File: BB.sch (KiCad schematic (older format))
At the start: 0 parts

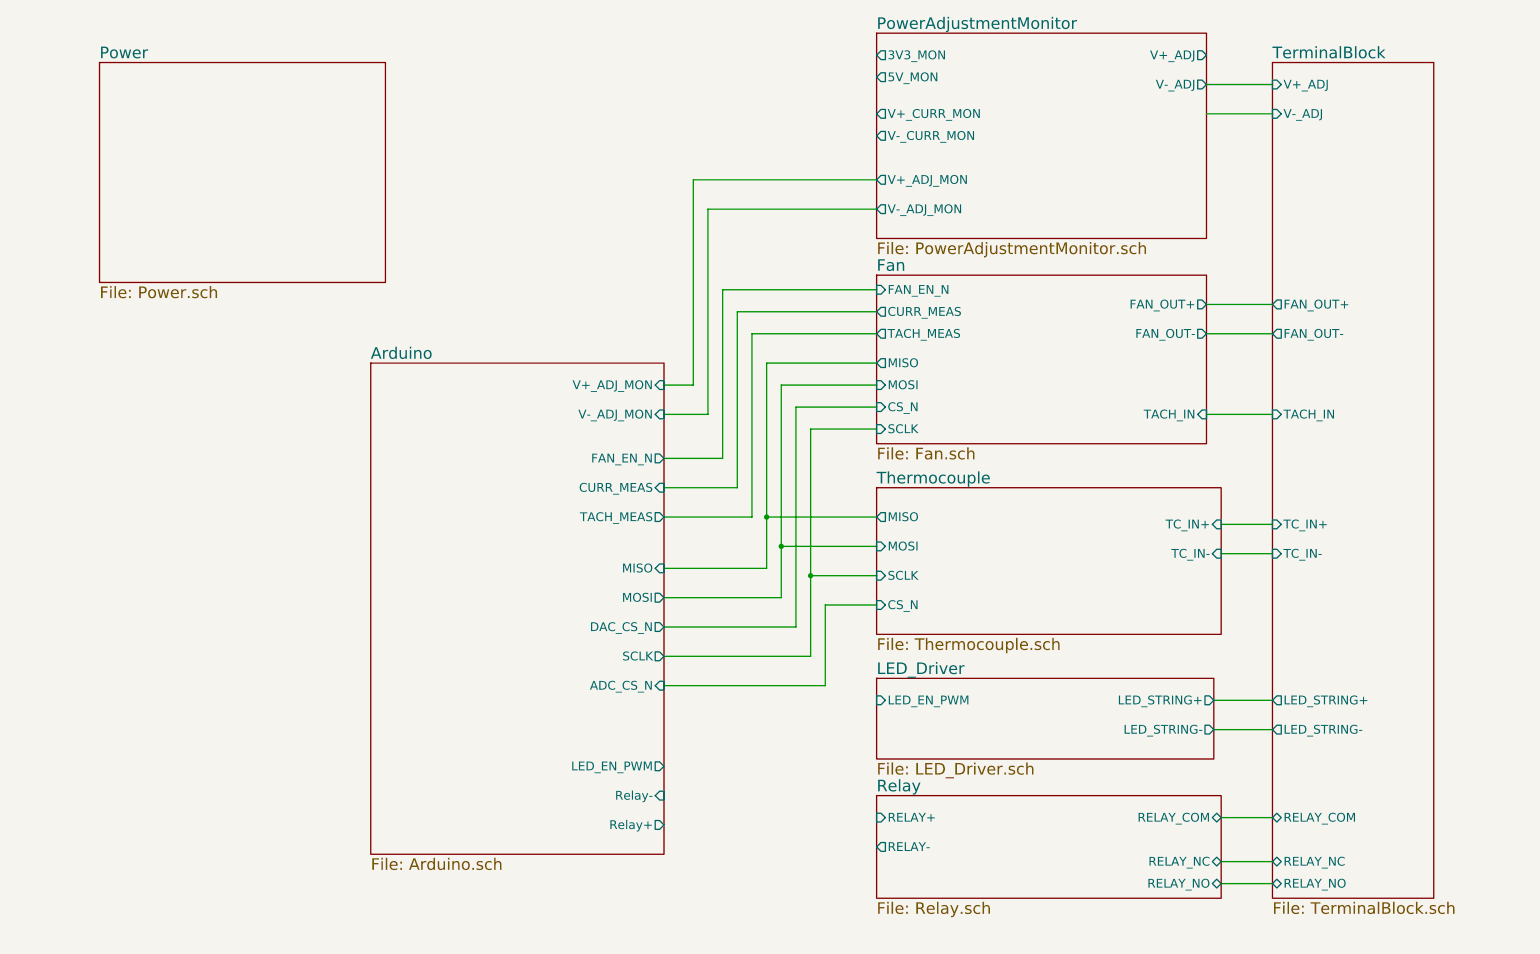
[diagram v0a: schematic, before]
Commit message: Week 3 changes. 	new file:   Arduino.sch 	modified:   BB-cache.lib 	new file:   BB.bck 	new file:   BB.dcm 	new file:   BB.lib 	modified:   BB.sch 	new file:   Fan.sch 	new file:   LED_Driver.sch 	new file:   Power.sch 	new file:   PowerAdjustmentMonitor.sch 	new file:   Relay.sch 	new file:   TerminalBlock.sch 	new file:   Thermocouple.sch
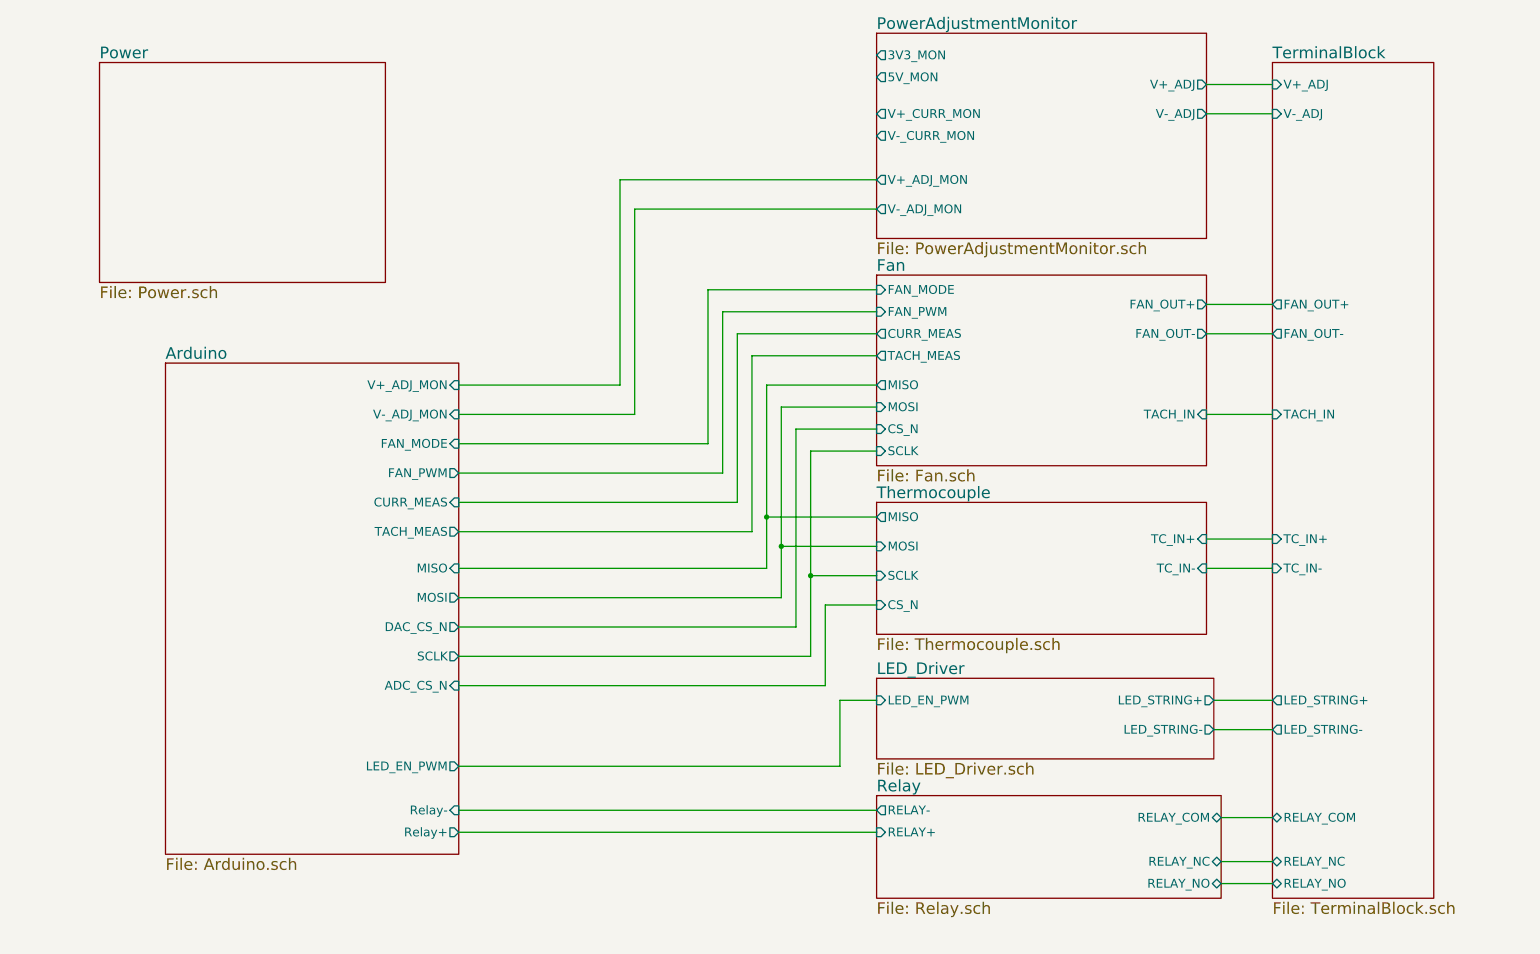
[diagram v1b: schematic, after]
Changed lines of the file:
@@
 F7 "LED_STRING+" O L 9250 5200 60
 F8 "LED_STRING-" O L 9250 5400 60
-F9 "TC_IN+" I L 9250 4000 60
-F10 "TC_IN-" I L 9250 4200 60
+F9 "TC_IN+" I L 9250 4100 60
+F10 "TC_IN-" I L 9250 4300 60
 F11 "RELAY_COM" B L 9250 6000 60
 F12 "RELAY_NC" B L 9250 6300 60
@@
 $EndSheet
 $Sheet
-S 6550 2300 2250 1150
+S 6550 2300 2250 1300
 U 52ED2315
 F0 "Fan" 79
 F1 "Fan.sch" 79
-F2 "SCLK" I L 6550 3350 60
-F3 "CS_N" I L 6550 3200 60
-F4 "MOSI" I L 6550 3050 60
-F5 "MISO" O L 6550 2900 60
+F2 "SCLK" I L 6550 3500 60
+F3 "CS_N" I L 6550 3350 60
+F4 "MOSI" I L 6550 3200 60
+F5 "MISO" O L 6550 3050 60
 F6 "FAN_OUT+" O R 8800 2500 60
 F7 "TACH_IN" I R 8800 3250 60
-F8 "TACH_MEAS" O L 6550 2700 60
-F9 "FAN_EN_N" I L 6550 2400 60
-F10 "CURR_MEAS" O L 6550 2550 60
-F11 "FAN_OUT-" O R 8800 2700 60
+F8 "TACH_MEAS" O L 6550 2850 60
+F9 "CURR_MEAS" O L 6550 2700 60
+F10 "FAN_OUT-" O R 8800 2700 60
+F11 "FAN_PWM" I L 6550 2550 60
+F12 "FAN_MODE" I L 6550 2400 60
 $EndSheet
 $Sheet
@@
 F3 "RELAY_NO" B R 8900 6450 60
 F4 "RELAY_COM" B R 8900 6000 60
-F5 "RELAY+" I L 6550 6000 60
-F6 "RELAY-" O L 6550 6200 60
+F5 "RELAY+" I L 6550 6100 60
+F6 "RELAY-" O L 6550 5950 60
 $EndSheet
 $Sheet
@@
 F0 "PowerAdjustmentMonitor" 79
 F1 "PowerAdjustmentMonitor.sch" 79
-F2 "V+_ADJ" O R 8800 800 60
-F3 "V-_ADJ" O R 8800 1000 60
+F2 "V+_ADJ" O R 8800 1000 60
+F3 "V-_ADJ" O R 8800 1200 60
 F4 "3V3_MON" O L 6550 800 60
 F5 "5V_MON" O L 6550 950 60
@@
 Wire Wire Line
 	8900 6450 9250 6450
-$Sheet
-S 3100 2900 2000 3350
-U 52ED2231
-F0 "Arduino" 79
-F1 "Arduino.sch" 79
-F2 "Relay+" O R 5100 6050 60
-F3 "Relay-" I R 5100 5850 60
-F4 "MOSI" O R 5100 4500 60
-F5 "MISO" I R 5100 4300 60
-F6 "SCLK" O R 5100 4900 60
-F7 "TACH_MEAS" O R 5100 3950 60
-F8 "FAN_EN_N" O R 5100 3550 60
-F9 "CURR_MEAS" I R 5100 3750 60
-F10 "V+_ADJ_MON" I R 5100 3050 60
-F11 "V-_ADJ_MON" I R 5100 3250 60
-F12 "LED_EN_PWM" O R 5100 5650 60
-F13 "DAC_CS_N" O R 5100 4700 60
-F14 "ADC_CS_N" I R 5100 5100 60
-$EndSheet
-Wire Wire Line
-	5100 3050 5300 3050
-Wire Wire Line
-	5100 3250 5400 3250
-Wire Wire Line
-	5300 3050 5300 1650
-Wire Wire Line
-	5300 1650 6550 1650
-Wire Wire Line
-	5400 3250 5400 1850
-Wire Wire Line
-	5400 1850 6550 1850
-Wire Wire Line
-	5100 3550 5500 3550
-Wire Wire Line
-	5500 3550 5500 2400
-Wire Wire Line
-	5500 2400 6550 2400
-Wire Wire Line
-	5100 3750 5600 3750
-Wire Wire Line
-	5600 3750 5600 2550
-Wire Wire Line
-	5600 2550 6550 2550
-Wire Wire Line
-	5100 3950 5700 3950
-Wire Wire Line
-	5700 3950 5700 2700
-Wire Wire Line
-	5700 2700 6550 2700
-Wire Wire Line
-	5100 4300 5800 4300
-Wire Wire Line
-	5800 4300 5800 2900
-Wire Wire Line
-	5800 2900 6550 2900
-Wire Wire Line
-	5100 4500 5900 4500
-Wire Wire Line
-	5900 4500 5900 3050
-Wire Wire Line
-	5900 3050 6550 3050
-Wire Wire Line
-	5100 4700 6000 4700
-Wire Wire Line
-	6000 4700 6000 3200
-Wire Wire Line
-	6000 3200 6550 3200
-Wire Wire Line
-	5100 4900 6100 4900
-Wire Wire Line
-	6100 4900 6100 3350
-Wire Wire Line
-	6100 3350 6550 3350
+Wire Wire Line
+	3700 3050 4800 3050
+Wire Wire Line
+	3700 3250 4900 3250
+Wire Wire Line
+	4800 3050 4800 1650
+Wire Wire Line
+	4800 1650 6550 1650
+Wire Wire Line
+	4900 3250 4900 1850
+Wire Wire Line
+	4900 1850 6550 1850
+Wire Wire Line
+	3700 3650 5500 3650
+Wire Wire Line
+	5500 3650 5500 2550
+Wire Wire Line
+	5500 2550 6550 2550
+Wire Wire Line
+	3700 3850 5600 3850
+Wire Wire Line
+	5600 3850 5600 2700
+Wire Wire Line
+	5600 2700 6550 2700
+Wire Wire Line
+	3700 4050 5700 4050
+Wire Wire Line
+	5700 4050 5700 2850
+Wire Wire Line
+	5700 2850 6550 2850
+Wire Wire Line
+	5800 4300 3700 4300
+Wire Wire Line
+	5800 3050 5800 4300
+Wire Wire Line
+	5800 3050 6550 3050
+Wire Wire Line
+	5900 4500 3700 4500
+Wire Wire Line
+	5900 3200 5900 4500
+Wire Wire Line
+	5900 3200 6550 3200
+Wire Wire Line
+	3700 4700 6000 4700
+Wire Wire Line
+	6000 4700 6000 3350
+Wire Wire Line
+	6000 3350 6550 3350
+Wire Wire Line
+	6100 4900 3700 4900
+Wire Wire Line
+	6100 3500 6100 4900
+Wire Wire Line
+	6100 3500 6550 3500
 Wire Wire Line
 	6550 4550 6200 4550
@@
 	6200 4550 6200 5100
 Wire Wire Line
-	6200 5100 5100 5100
-Wire Wire Line
-	9250 4000 8900 4000
-Wire Wire Line
-	9250 4200 8900 4200
+	6200 5100 3700 5100
 Wire Wire Line
 	9250 5200 8850 5200
@@
 	9250 5400 8850 5400
 $Sheet
-S 6550 3750 2350 1000
+S 6550 3850 2250 900
 U 52ED22BF
 F0 "Thermocouple" 79
@@
 F4 "SCLK" I L 6550 4350 60
 F5 "CS_N" I L 6550 4550 60
-F6 "TC_IN+" I R 8900 4000 60
-F7 "TC_IN-" I R 8900 4200 60
+F6 "TC_IN+" I R 8800 4100 60
+F7 "TC_IN-" I R 8800 4300 60
 $EndSheet
 Wire Wire Line
@@
 	6550 4350 6100 4350
 Connection ~ 6100 4350
+$Sheet
+S 1700 2900 2000 3350
+U 52ED2231
+F0 "Arduino" 79
+F1 "Arduino.sch" 79
+F2 "Relay+" O R 3700 6100 60
+F3 "Relay-" I R 3700 5950 60
+F4 "MOSI" O R 3700 4500 60
+F5 "MISO" I R 3700 4300 60
+F6 "SCLK" O R 3700 4900 60
+F7 "TACH_MEAS" O R 3700 4050 60
+F8 "FAN_PWM" O R 3700 3650 60
+F9 "CURR_MEAS" I R 3700 3850 60
+F10 "V+_ADJ_MON" I R 3700 3050 60
+F11 "V-_ADJ_MON" I R 3700 3250 60
+F12 "LED_EN_PWM" O R 3700 5650 60
+F13 "DAC_CS_N" O R 3700 4700 60
+F14 "ADC_CS_N" I R 3700 5100 60
+F15 "FAN_MODE" I R 3700 3450 60
+$EndSheet
+Wire Wire Line
+	3700 3450 5400 3450
+Wire Wire Line
+	5400 3450 5400 2400
+Wire Wire Line
+	5400 2400 6550 2400
+Wire Wire Line
+	6550 5200 6300 5200
+Wire Wire Line
+	6300 5200 6300 5650
+Wire Wire Line
+	6300 5650 3700 5650
+Wire Wire Line
+	3700 5950 6550 5950
+Wire Wire Line
+	6550 6100 3700 6100
+Wire Wire Line
+	9250 4100 8800 4100
+Wire Wire Line
+	8800 4300 9250 4300
 $EndSCHEMATC

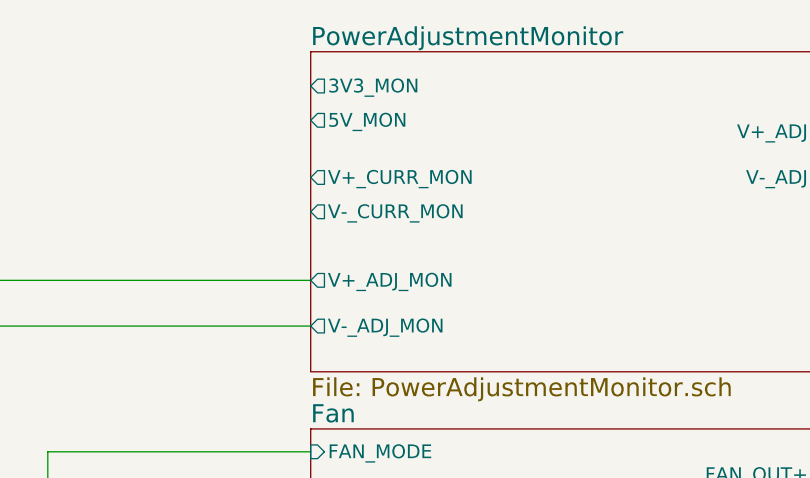
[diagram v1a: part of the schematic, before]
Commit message: Added Relay module footprints.
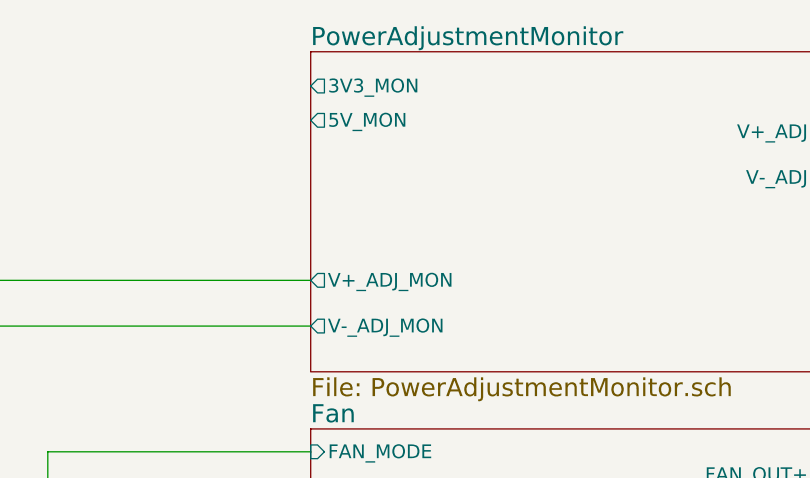
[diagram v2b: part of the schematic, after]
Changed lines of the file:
@@
 LIBS:valves
 LIBS:BB
+LIBS:GLSP
 LIBS:BB-cache
 EELAYER 24 0
@@
 F6 "V+_ADJ_MON" O L 6550 1650 60
 F7 "V-_ADJ_MON" O L 6550 1850 60
-F8 "V+_CURR_MON" O L 6550 1200 60
-F9 "V-_CURR_MON" O L 6550 1350 60
 $EndSheet
 Wire Wire Line

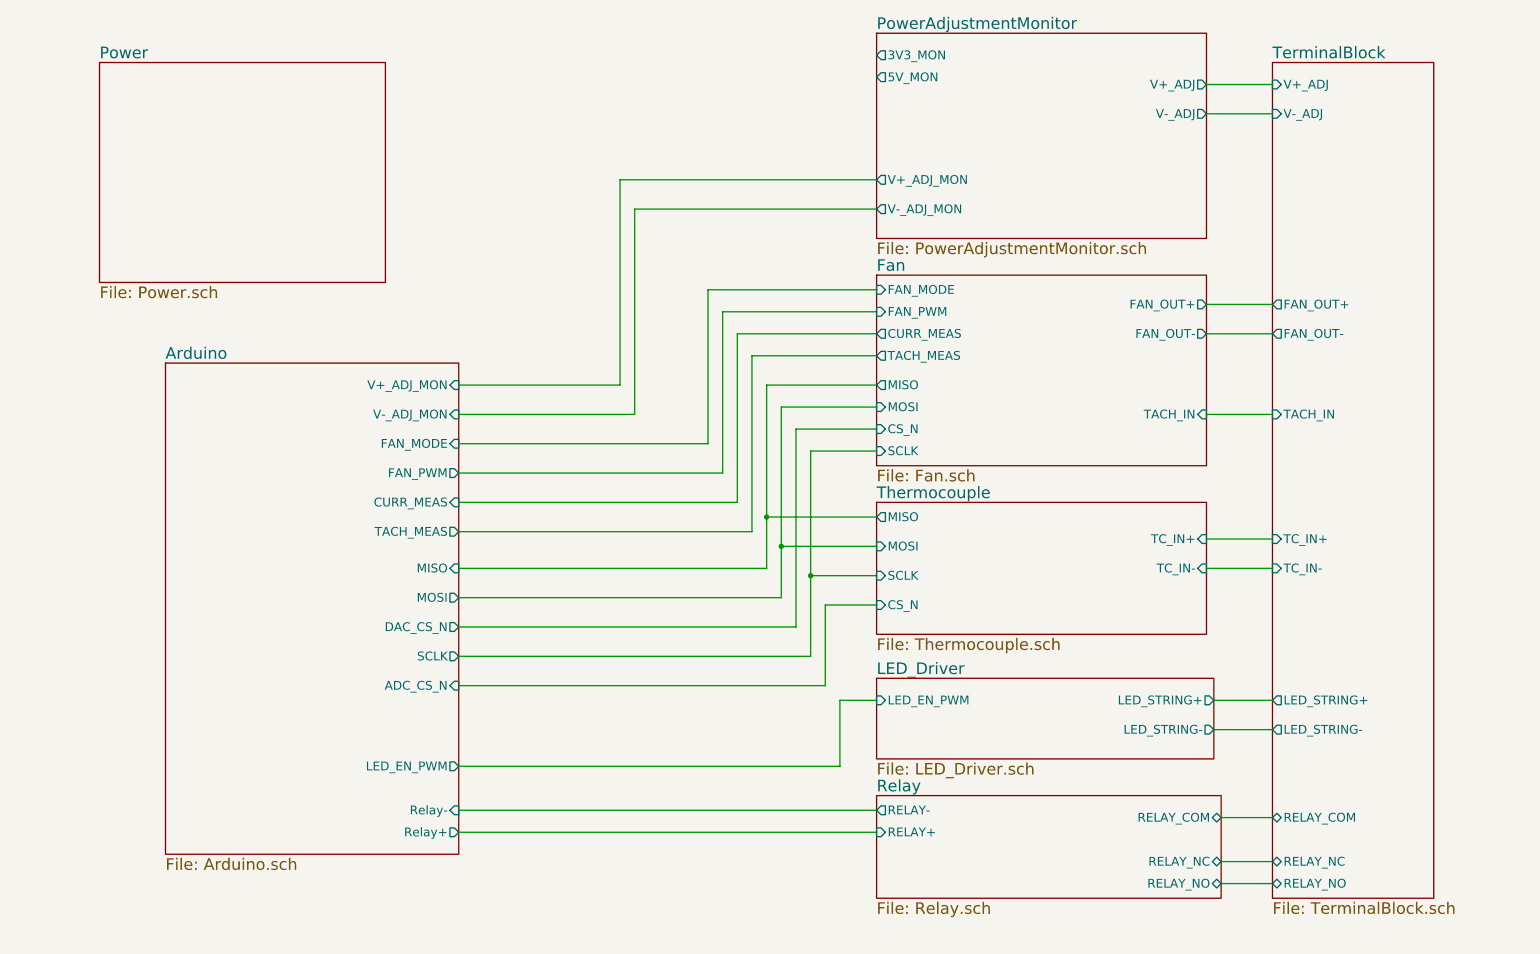
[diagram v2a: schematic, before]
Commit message: Associated and placed thermocouple, terminal, arduino, fan driver, power protection modules.
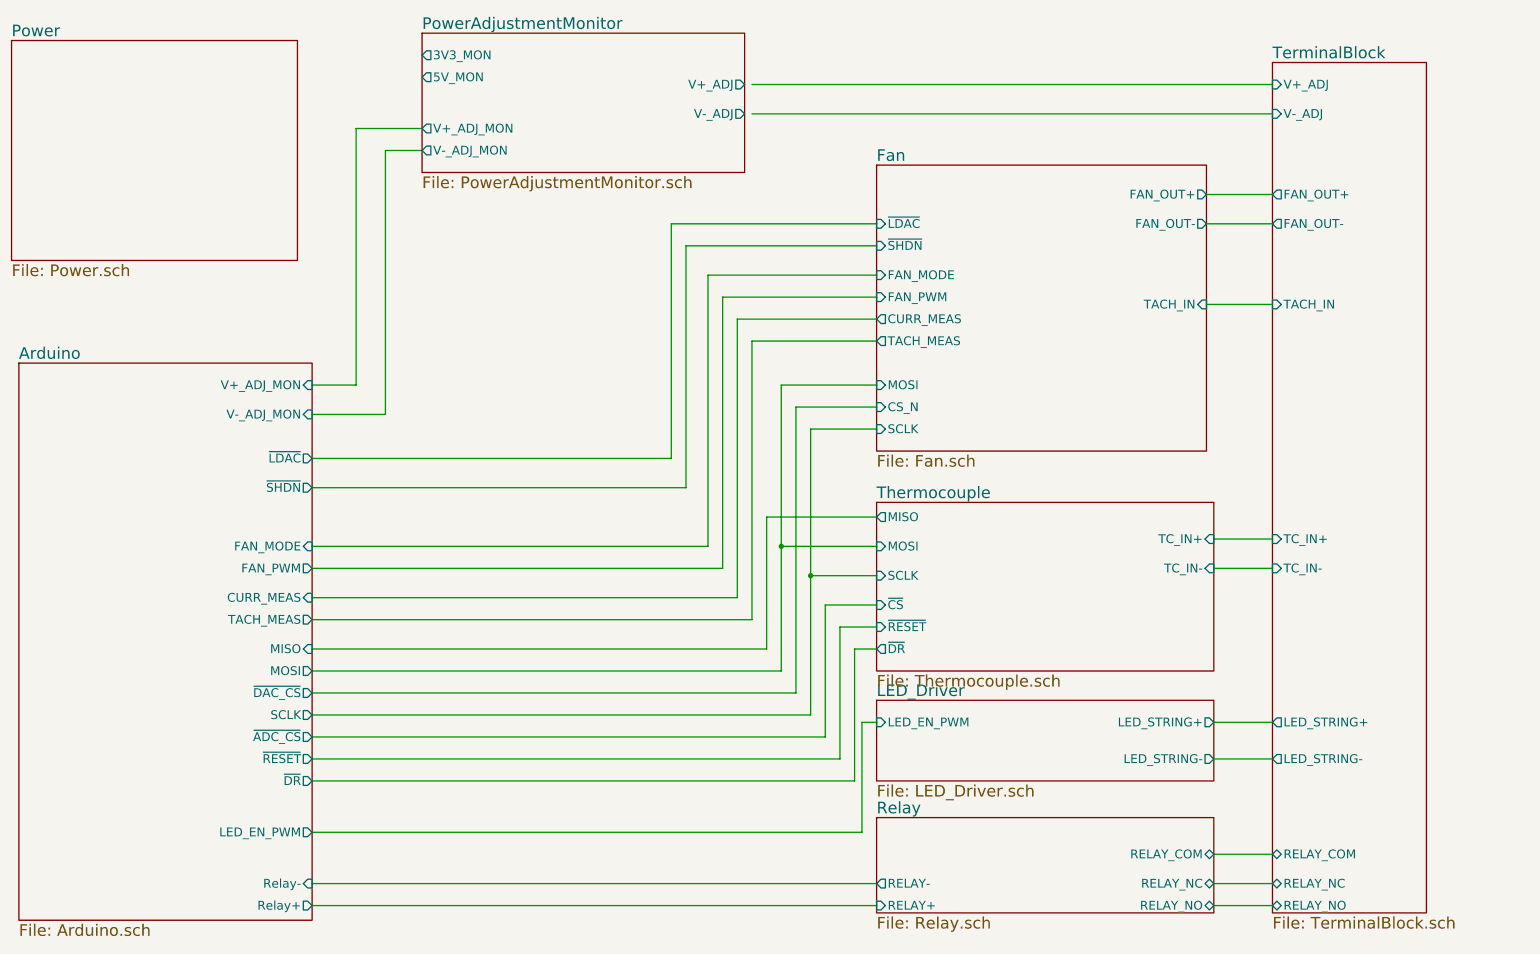
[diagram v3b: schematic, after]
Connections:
- wire segments 53 -> 64

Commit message: Layout sessions 1-4.
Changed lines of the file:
@@
 $EndSheet
 Wire Wire Line
-	9250 1000 5700 1000
+	5650 1000 9250 1000
 Wire Wire Line
-	5700 1200 9250 1200
+	5650 1200 9250 1200
 Wire Wire Line
 	8850 6450 9250 6450
